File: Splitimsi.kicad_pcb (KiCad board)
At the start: 2 copper layers, 118.2 x 99.3 mm, 30 parts, among them SW1 MX_RGB, SW10 MX_RGB, SW11 MX_RGB, SW12 MX_RGB, SW13 MX_RGB, SW14 MX_RGB, SW15 MX_RGB, SW16 MX_RGB, SW17 MX_RGB, SW18 MX_RGB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

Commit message: Minor Adjustments
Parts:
- moved S1 7.39 mm to (126.4, 72.5), turned to 90 degrees
- moved SW27 0.99 mm to (127.0, 104.8)
- moved SW21 0.92 mm to (127.0, 85.7)
- moved SW26 0.90 mm to (108.0, 104.8)
- moved SW20 0.81 mm to (108.0, 85.7)
- moved SW25 0.81 mm to (88.9, 104.8)
- moved SW15 0.74 mm to (108.0, 66.7)
- moved SW24 0.74 mm to (69.8, 104.8)
- moved SW19 0.72 mm to (88.9, 85.7)
- moved SW23 0.68 mm to (50.8, 104.8)
- moved SW10 0.68 mm to (108.0, 47.6)
- moved SW5 0.65 mm to (108.0, 28.6)
- moved SW22 0.65 mm to (31.8, 104.8)
- moved SW18 0.64 mm to (69.8, 85.7)
- moved SW14 0.63 mm to (88.9, 66.7)
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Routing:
- net Net-(SW21-Pad6): track 0.00 -> 135.2 mm
- net Net-(SW24-Pad6): track 14.8 -> 0.00 mm, vias 1 -> 0
- net Net-(SW4-Pad6): track 14.6 -> 0.00 mm
- net Net-(SW3-Pad6): track 14.6 -> 0.00 mm
- net Net-(SW26-Pad6): track 14.6 -> 0.00 mm
- net Net-(SW23-Pad6): track 14.6 -> 0.00 mm
- net Net-(SW22-Pad6): track 14.6 -> 0.00 mm
- net Net-(SW20-Pad6): track 14.6 -> 0.00 mm
- net Net-(SW2-Pad6): track 14.6 -> 0.00 mm
- net Net-(SW18-Pad6): track 14.6 -> 0.00 mm
- net Net-(SW16-Pad6): track 14.6 -> 0.00 mm
- net Net-(SW14-Pad6): track 14.6 -> 0.00 mm
- net Net-(SW13-Pad6): track 14.6 -> 0.00 mm
- net Net-(SW11-Pad6): track 14.6 -> 0.00 mm
- net Net-(SW1-Pad6): track 14.6 -> 0.00 mm
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
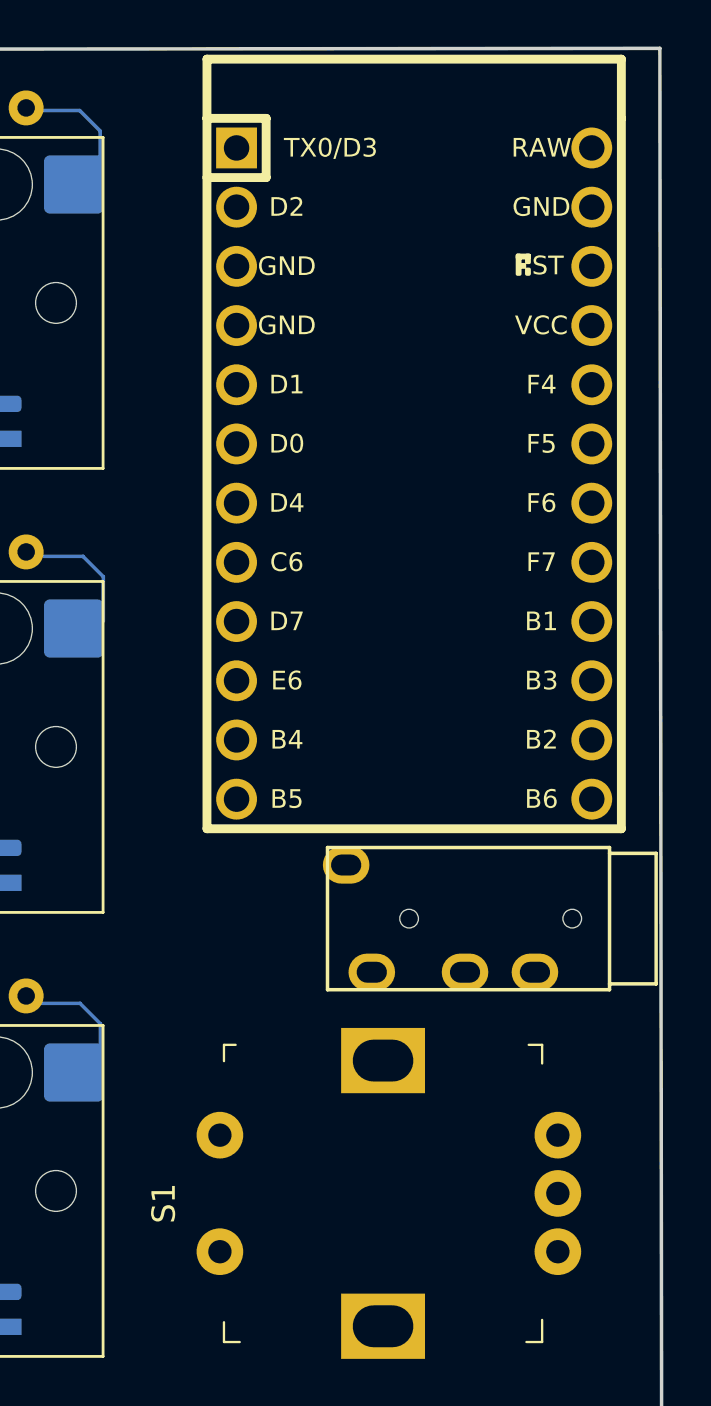
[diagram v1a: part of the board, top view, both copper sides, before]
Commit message: diode 3d models added
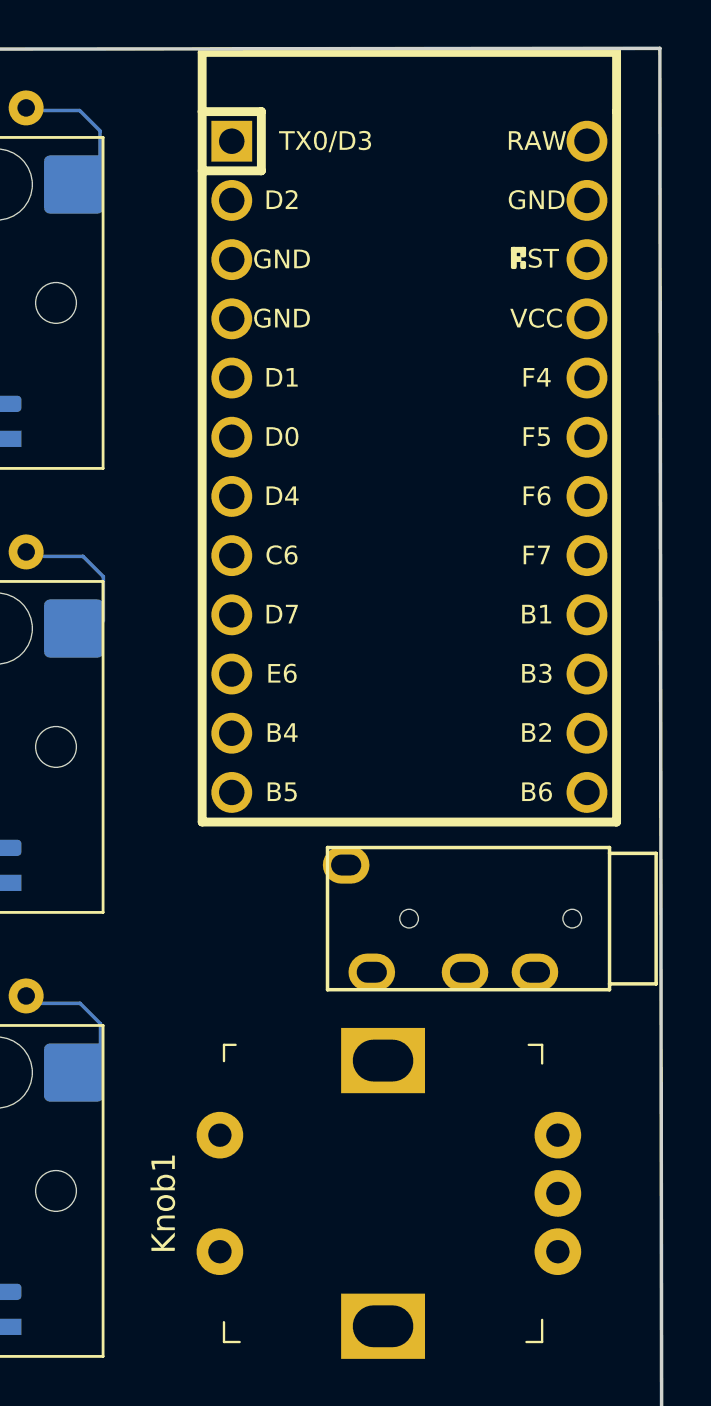
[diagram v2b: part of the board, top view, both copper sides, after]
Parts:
- moved U1 0.35 mm to (127.6, 35.6)
- renumbered S1 to Knob1
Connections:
- net /Col 0 renamed /Col0
- net /Col 1 renamed /Col1
- net /Col 3 renamed /Col3
- net /Col 4 renamed /Col4
- net /Row 0 renamed /Row0
- net /Row 1 renamed /Row1
- net /Row 2 renamed /Row2
- net /Row 3 renamed /Row3
- net /Row 4 renamed /Row4
- Knob1 pad 1: unconnected-(S1-Pad1) -> /Col5
- SW1 pad 6: Net-(SW1-Pad6) -> unconnected-(SW1-Pad6)
- SW10 pad 4: Net-(SW10-Pad4) -> unconnected-(SW10-Pad4)
- SW10 pad 6: Net-(SW10-Pad6) -> unconnected-(SW10-Pad6)
- SW11 pad 4: Net-(SW10-Pad6) -> unconnected-(SW11-Pad4)
- SW11 pad 6: Net-(SW11-Pad6) -> unconnected-(SW11-Pad6)
- SW12 pad 4: Net-(SW11-Pad6) -> unconnected-(SW12-Pad4)
- SW12 pad 6: /Col 2 -> unconnected-(SW12-Pad6)
- SW13 pad 1: /Col 2 -> /Col2
- SW13 pad 4: /Col 2 -> unconnected-(SW13-Pad4)
- SW13 pad 6: Net-(SW13-Pad6) -> unconnected-(SW13-Pad6)
- SW14 pad 4: Net-(SW13-Pad6) -> unconnected-(SW14-Pad4)
- SW14 pad 6: Net-(SW14-Pad6) -> unconnected-(SW14-Pad6)
- SW15 pad 4: Net-(SW14-Pad6) -> unconnected-(SW15-Pad4)
- SW15 pad 6: Net-(SW15-Pad6) -> unconnected-(SW15-Pad6)
- SW16 pad 4: Net-(SW15-Pad6) -> unconnected-(SW16-Pad4)
- SW16 pad 6: Net-(SW16-Pad6) -> unconnected-(SW16-Pad6)
- SW17 pad 4: Net-(SW16-Pad6) -> unconnected-(SW17-Pad4)
- SW17 pad 6: Net-(SW17-Pad6) -> unconnected-(SW17-Pad6)
- SW18 pad 1: /Col 2 -> /Col2
- SW18 pad 4: Net-(SW17-Pad6) -> unconnected-(SW18-Pad4)
- SW18 pad 6: Net-(SW18-Pad6) -> unconnected-(SW18-Pad6)
- SW19 pad 4: Net-(SW18-Pad6) -> unconnected-(SW19-Pad4)
- SW19 pad 6: Net-(SW19-Pad6) -> unconnected-(SW19-Pad6)
- SW2 pad 4: Net-(SW1-Pad6) -> unconnected-(SW2-Pad4)
- SW2 pad 6: Net-(SW2-Pad6) -> unconnected-(SW2-Pad6)
- SW20 pad 4: Net-(SW19-Pad6) -> unconnected-(SW20-Pad4)
- SW20 pad 6: Net-(SW20-Pad6) -> unconnected-(SW20-Pad6)
- SW21 pad 1: /Col 5 -> /Col5
- SW21 pad 4: Net-(SW20-Pad6) -> unconnected-(SW21-Pad4)
- SW21 pad 6: Net-(SW21-Pad6) -> unconnected-(SW21-Pad6)
- SW22 pad 4: Net-(SW21-Pad6) -> unconnected-(SW22-Pad4)
- SW22 pad 6: Net-(SW22-Pad6) -> unconnected-(SW22-Pad6)
- SW23 pad 4: Net-(SW22-Pad6) -> unconnected-(SW23-Pad4)
- SW23 pad 6: Net-(SW23-Pad6) -> unconnected-(SW23-Pad6)
- SW24 pad 1: /Col 2 -> /Col2
- SW24 pad 4: Net-(SW23-Pad6) -> unconnected-(SW24-Pad4)
- SW24 pad 6: Net-(SW24-Pad6) -> unconnected-(SW24-Pad6)
- SW25 pad 4: Net-(SW24-Pad6) -> unconnected-(SW25-Pad4)
- SW25 pad 6: Net-(SW25-Pad6) -> unconnected-(SW25-Pad6)
- SW26 pad 4: Net-(SW25-Pad6) -> unconnected-(SW26-Pad4)
- SW26 pad 6: Net-(SW26-Pad6) -> unconnected-(SW26-Pad6)
- SW27 pad 1: /Col 5 -> /Col5
- SW27 pad 4: Net-(SW26-Pad6) -> unconnected-(SW27-Pad4)
- SW3 pad 1: /Col 2 -> /Col2
- SW3 pad 4: Net-(SW2-Pad6) -> unconnected-(SW3-Pad4)
- SW3 pad 6: Net-(SW3-Pad6) -> unconnected-(SW3-Pad6)
- SW4 pad 4: Net-(SW3-Pad6) -> unconnected-(SW4-Pad4)
- SW4 pad 6: Net-(SW4-Pad6) -> unconnected-(SW4-Pad6)
- SW5 pad 4: Net-(SW4-Pad6) -> unconnected-(SW5-Pad4)
- SW5 pad 6: Net-(SW5-Pad6) -> unconnected-(SW5-Pad6)
- SW6 pad 4: Net-(SW5-Pad6) -> unconnected-(SW6-Pad4)
- SW6 pad 6: Net-(SW6-Pad6) -> unconnected-(SW6-Pad6)
- SW7 pad 4: Net-(SW6-Pad6) -> unconnected-(SW7-Pad4)
- SW7 pad 6: Net-(SW7-Pad6) -> unconnected-(SW7-Pad6)
- SW8 pad 1: /Col 2 -> /Col2
- SW8 pad 4: Net-(SW7-Pad6) -> unconnected-(SW8-Pad4)
- SW8 pad 6: Net-(SW8-Pad6) -> unconnected-(SW8-Pad6)
- SW9 pad 4: Net-(SW8-Pad6) -> unconnected-(SW9-Pad4)
- SW9 pad 6: Net-(SW10-Pad4) -> unconnected-(SW9-Pad6)
- U1 pad 21: unconnected-(U1-Pad21) -> +5V
- U1 pad 23: unconnected-(U1-Pad23) -> GND
- U1 pad 3: unconnected-(U1-Pad3) -> GND
- U1 pad 4: unconnected-(U1-Pad4) -> GND
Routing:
- net unconnected-(SW21-Pad6): track 0.00 -> 135.2 mm
- net Net-(SW21-Pad6): track 135.2 -> 0.00 mm

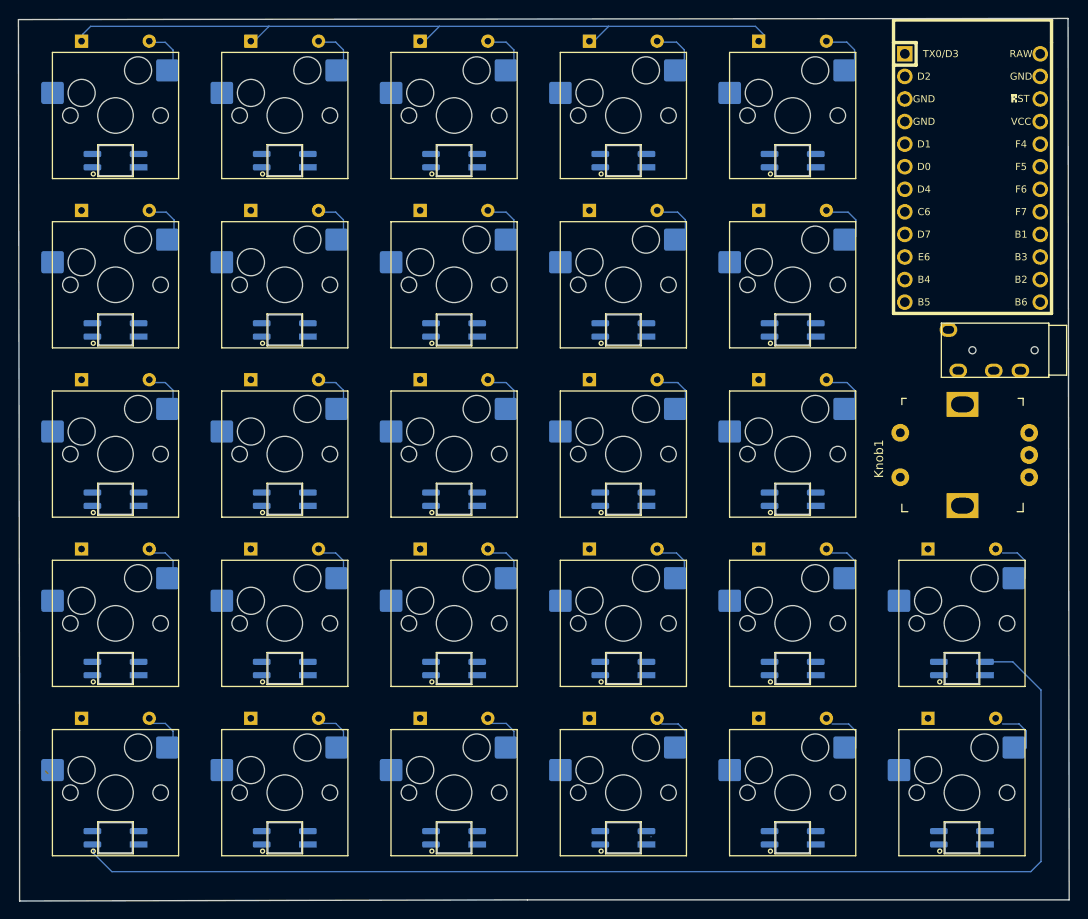
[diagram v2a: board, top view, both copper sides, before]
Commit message: v0.3
- Led footprints corrected and rearranged
- Knob, Led, ProMicro, TRRS 3d models fine tuned
- Led Labels added
- Same row Leds connected
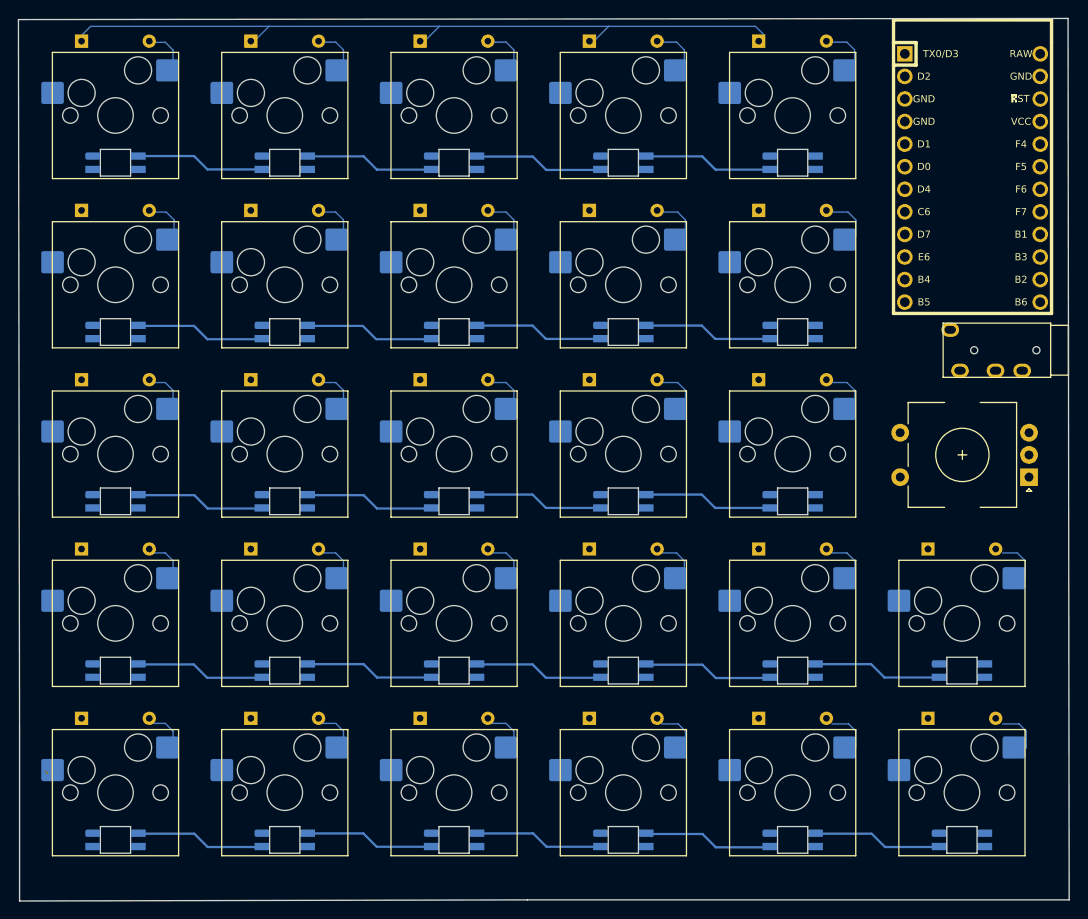
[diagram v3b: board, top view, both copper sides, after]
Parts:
- Knob1: value PEC11R-4215F-S0024 -> RotaryEncoder_Switch; footprint digikey-footprints:Rotary_Encoder_Switched_PEC11R -> Keebio-Parts:RotaryEncoder_EC11
- moved Knob1 5.71 mm to (126.4, 66.8), turned to 180 degrees
- moved U2 0.20 mm to (136.3, 55.0)
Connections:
- SW1 pad 4: unconnected-(SW1-Pad4) -> Net-(SW1-Pad4)
- SW10 pad 4: unconnected-(SW10-Pad4) -> /Row1_LedOut
- SW10 pad 6: unconnected-(SW10-Pad6) -> Net-(SW10-Pad6)
- SW11 pad 4: unconnected-(SW11-Pad4) -> Net-(SW11-Pad4)
- SW11 pad 6: unconnected-(SW11-Pad6) -> /Row1_LedOut
- SW12 pad 4: unconnected-(SW12-Pad4) -> Net-(SW12-Pad4)
- SW12 pad 6: unconnected-(SW12-Pad6) -> Net-(SW11-Pad4)
- SW13 pad 4: unconnected-(SW13-Pad4) -> Net-(SW13-Pad4)
- SW13 pad 6: unconnected-(SW13-Pad6) -> Net-(SW12-Pad4)
- SW14 pad 4: unconnected-(SW14-Pad4) -> Net-(SW14-Pad4)
- SW14 pad 6: unconnected-(SW14-Pad6) -> Net-(SW13-Pad4)
- SW15 pad 4: unconnected-(SW15-Pad4) -> /Row2_LedOut
- SW15 pad 6: unconnected-(SW15-Pad6) -> Net-(SW14-Pad4)
- SW16 pad 4: unconnected-(SW16-Pad4) -> Net-(SW16-Pad4)
- SW16 pad 6: unconnected-(SW16-Pad6) -> /Row2_LedOut
- SW17 pad 4: unconnected-(SW17-Pad4) -> Net-(SW17-Pad4)
- SW17 pad 6: unconnected-(SW17-Pad6) -> Net-(SW16-Pad4)
- SW18 pad 4: unconnected-(SW18-Pad4) -> Net-(SW18-Pad4)
- SW18 pad 6: unconnected-(SW18-Pad6) -> Net-(SW17-Pad4)
- SW19 pad 4: unconnected-(SW19-Pad4) -> Net-(SW19-Pad4)
- SW19 pad 6: unconnected-(SW19-Pad6) -> Net-(SW18-Pad4)
- SW2 pad 4: unconnected-(SW2-Pad4) -> Net-(SW2-Pad4)
- SW2 pad 6: unconnected-(SW2-Pad6) -> Net-(SW1-Pad4)
- SW20 pad 4: unconnected-(SW20-Pad4) -> Net-(SW20-Pad4)
- SW20 pad 6: unconnected-(SW20-Pad6) -> Net-(SW19-Pad4)
- SW21 pad 4: unconnected-(SW21-Pad4) -> /Row3_LedOut
- SW21 pad 6: unconnected-(SW21-Pad6) -> Net-(SW20-Pad4)
- SW22 pad 4: unconnected-(SW22-Pad4) -> Net-(SW22-Pad4)
- SW22 pad 6: unconnected-(SW22-Pad6) -> /Row3_LedOut
- SW23 pad 4: unconnected-(SW23-Pad4) -> Net-(SW23-Pad4)
- SW23 pad 6: unconnected-(SW23-Pad6) -> Net-(SW22-Pad4)
- SW24 pad 4: unconnected-(SW24-Pad4) -> Net-(SW24-Pad4)
- SW24 pad 6: unconnected-(SW24-Pad6) -> Net-(SW23-Pad4)
- SW25 pad 4: unconnected-(SW25-Pad4) -> Net-(SW25-Pad4)
- SW25 pad 6: unconnected-(SW25-Pad6) -> Net-(SW24-Pad4)
- SW26 pad 4: unconnected-(SW26-Pad4) -> Net-(SW26-Pad4)
- SW26 pad 6: unconnected-(SW26-Pad6) -> Net-(SW25-Pad4)
- SW27 pad 4: unconnected-(SW27-Pad4) -> /Row4_LedOut
- SW27 pad 6: unconnected-(SW27-Pad6) -> Net-(SW26-Pad4)
- SW3 pad 4: unconnected-(SW3-Pad4) -> Net-(SW3-Pad4)
- SW3 pad 6: unconnected-(SW3-Pad6) -> Net-(SW2-Pad4)
- SW4 pad 4: unconnected-(SW4-Pad4) -> Net-(SW4-Pad4)
- SW4 pad 6: unconnected-(SW4-Pad6) -> Net-(SW3-Pad4)
- SW5 pad 4: unconnected-(SW5-Pad4) -> /Row0_LedOut
- SW5 pad 6: unconnected-(SW5-Pad6) -> Net-(SW4-Pad4)
- SW6 pad 4: unconnected-(SW6-Pad4) -> Net-(SW6-Pad4)
- SW6 pad 6: unconnected-(SW6-Pad6) -> /Row0_LedOut
- SW7 pad 4: unconnected-(SW7-Pad4) -> Net-(SW7-Pad4)
- SW7 pad 6: unconnected-(SW7-Pad6) -> Net-(SW6-Pad4)
- SW8 pad 4: unconnected-(SW8-Pad4) -> Net-(SW8-Pad4)
- SW8 pad 6: unconnected-(SW8-Pad6) -> Net-(SW7-Pad4)
- SW9 pad 4: unconnected-(SW9-Pad4) -> Net-(SW10-Pad6)
- SW9 pad 6: unconnected-(SW9-Pad6) -> Net-(SW8-Pad4)
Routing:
- net unconnected-(SW21-Pad6): track 135.2 -> 0.00 mm
- net Net-(SW25-Pad4): track 0.00 -> 14.6 mm
- net Net-(SW4-Pad4): track 0.00 -> 14.6 mm
- net Net-(SW3-Pad4): track 0.00 -> 14.6 mm
- net Net-(SW24-Pad4): track 0.00 -> 14.6 mm
- net Net-(SW2-Pad4): track 0.00 -> 14.6 mm
- net Net-(SW17-Pad4): track 0.00 -> 14.6 mm
- net Net-(SW16-Pad4): track 0.00 -> 14.6 mm
- net Net-(SW12-Pad4): track 0.00 -> 14.6 mm
- net Net-(SW1-Pad4): track 0.00 -> 14.6 mm
- net Net-(SW7-Pad4): track 0.00 -> 14.6 mm
- net Net-(SW6-Pad4): track 0.00 -> 14.6 mm
- net Net-(SW23-Pad4): track 0.00 -> 14.6 mm
- net Net-(SW22-Pad4): track 0.00 -> 14.6 mm
- net Net-(SW11-Pad4): track 0.00 -> 14.6 mm
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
